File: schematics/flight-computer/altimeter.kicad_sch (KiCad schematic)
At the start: 17 parts, among them U201 NXB0108PW-Q100J, U202 ICM-20789, U203 MS5611-01BA, U204 PCA9306

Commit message: Add order codes for remaining components
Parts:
- C202, C203, C208: Farnell (none) -> 9402047
- R201: Farnell (none) -> 2059185
- R202, R203, R204, R205: Farnell (none) -> 2447187
- U201: Farnell (none) -> 3585605
- U204: Farnell (none) -> 2845091
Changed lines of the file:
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@@
+      (effects (font (size 1.27 1.27)) hide)
+    )
+    (property "Farnell" "2447187" (id 4) (at 129.54 139.7 0)
+      (effects (font (size 1.27 1.27)) hide)
+    )
+    (property "Mouser" "~" (id 5) (at 129.54 139.7 0)
+      (effects (font (size 1.27 1.27)) hide)
+    )
+    (property "RS" "~" (id 6) (at 129.54 139.7 0)
       (effects (font (size 1.27 1.27)) hide)
     )
@@
       (effects (font (size 1.27 1.27)) hide)
     )
+    (property "Mouser" "~" (id 5) (at 176.53 76.2 0)
+      (effects (font (size 1.27 1.27)) hide)
+    )
+    (property "RS" "~" (id 6) (at 176.53 76.2 0)
+      (effects (font (size 1.27 1.27)) hide)
+    )
     (pin "1")
     (pin "2")
@@
       (effects (font (size 1.27 1.27)) hide)
     )
-    (property "Farnell" "" (id 4) (at 105.41 104.14 0)
+    (property "Farnell" "9402047" (id 4) (at 105.41 104.14 0)
+      (effects (font (size 1.27 1.27)) hide)
+    )
+    (property "Mouser" "~" (id 5) (at 105.41 104.14 0)
+      (effects (font (size 1.27 1.27)) hide)
+    )
+    (property "RS" "~" (id 6) (at 105.41 104.14 0)
       (effects (font (size 1.27 1.27)) hide)
     )
@@
     )
     (property "Datasheet" "http://www.ti.com/lit/ds/symlink/pca9306.pdf" (id 3) (at 120.65 135.89 0)
+      (effects (font (size 1.27 1.27)) hide)
+    )
+    (property "Farnell" "2845091" (id 4) (at 113.03 147.32 0)
+      (effects (font (size 1.27 1.27)) hide)
+    )
+    (property "Mouser" "~" (id 5) (at 113.03 147.32 0)
+      (effects (font (size 1.27 1.27)) hide)
+    )
+    (property "RS" "~" (id 6) (at 113.03 147.32 0)
       (effects (font (size 1.27 1.27)) hide)
     )
@@
       (effects (font (size 1.27 1.27)) hide)
     )
+    (property "Mouser" "~" (id 5) (at 162.56 104.14 0)
+      (effects (font (size 1.27 1.27)) hide)
+    )
+    (property "RS" "~" (id 6) (at 162.56 104.14 0)
+      (effects (font (size 1.27 1.27)) hide)
+    )
     (pin "1")
     (pin "2")
@@
     )
     (property "Farnell" "9402047" (id 4) (at 229.87 104.14 0)
+      (effects (font (size 1.27 1.27)) hide)
+    )
+    (property "Mouser" "~" (id 5) (at 229.87 104.14 0)
+      (effects (font (size 1.27 1.27)) hide)
+    )
+    (property "RS" "~" (id 6) (at 229.87 104.14 0)
       (effects (font (size 1.27 1.27)) hide)
     )
@@
       (effects (font (size 1.27 1.27)) hide)
     )
+    (property "Farnell" "2447187" (id 4) (at 132.08 139.7 0)
+      (effects (font (size 1.27 1.27)) hide)
+    )
+    (property "Mouser" "~" (id 5) (at 132.08 139.7 0)
+      (effects (font (size 1.27 1.27)) hide)
+    )
+    (property "RS" "~" (id 6) (at 132.08 139.7 0)
+      (effects (font (size 1.27 1.27)) hide)
+    )
     (pin "1")
     (pin "2")
@@
       (effects (font (size 1.27 1.27)) hide)
     )
-    (property "Farnell" "" (id 4) (at 101.6 156.21 0)
+    (property "Farnell" "9402047" (id 4) (at 101.6 156.21 0)
+      (effects (font (size 1.27 1.27)) hide)
+    )
+    (property "Mouser" "~" (id 5) (at 101.6 156.21 0)
+      (effects (font (size 1.27 1.27)) hide)
+    )
+    (property "RS" "~" (id 6) (at 101.6 156.21 0)
       (effects (font (size 1.27 1.27)) hide)
     )
@@
       (effects (font (size 1.27 1.27)) hide)
     )
+    (property "Mouser" "~" (id 5) (at 157.48 104.14 0)
+      (effects (font (size 1.27 1.27)) hide)
+    )
+    (property "RS" "~" (id 6) (at 157.48 104.14 0)
+      (effects (font (size 1.27 1.27)) hide)
+    )
     (pin "1")
     (pin "2")
@@
     )
     (property "Datasheet" "" (id 3) (at 111.76 60.325 0)
+      (effects (font (size 1.27 1.27)) hide)
+    )
+    (property "Farnell" "3585605" (id 4) (at 111.76 62.23 0)
+      (effects (font (size 1.27 1.27)) hide)
+    )
+    (property "Mouser" "~" (id 5) (at 111.76 62.23 0)
+      (effects (font (size 1.27 1.27)) hide)
+    )
+    (property "RS" "~" (id 6) (at 111.76 62.23 0)
       (effects (font (size 1.27 1.27)) hide)
     )
@@
     )
     (property "Datasheet" "https://3cfeqx1hf82y3xcoull08ihx-wpengine.netdna-ssl.com/wp-content/uploads/2017/10/DS-000169-ICM-20789-TYP-v1.4.pdf" (id 3) (at 162.56 90.17 0)
+      (effects (font (size 1.27 1.27)) hide)
+    )
+    (property "Farnell" "~" (id 4) (at 162.56 62.23 0)
+      (effects (font (size 1.27 1.27)) hide)
+    )
+    (property "Mouser" "~" (id 5) (at 162.56 62.23 0)
+      (effects (font (size 1.27 1.27)) hide)
+    )
+    (property "RS" "~" (id 6) (at 162.56 62.23 0)
       (effects (font (size 1.27 1.27)) hide)
     )
@@
       (effects (font (size 1.27 1.27)) hide)
     )
+    (property "Mouser" "~" (id 5) (at 171.45 104.14 0)
+      (effects (font (size 1.27 1.27)) hide)
+    )
+    (property "RS" "~" (id 6) (at 171.45 104.14 0)
+      (effects (font (size 1.27 1.27)) hide)
+    )
     (pin "1")
     (pin "2")
@@
       (effects (font (size 1.27 1.27)) hide)
     )
-    (property "Farnell" "" (id 4) (at 116.84 104.14 0)
+    (property "Farnell" "9402047" (id 4) (at 116.84 104.14 0)
+      (effects (font (size 1.27 1.27)) hide)
+    )
+    (property "Mouser" "~" (id 5) (at 116.84 104.14 0)
+      (effects (font (size 1.27 1.27)) hide)
+    )
+    (property "RS" "~" (id 6) (at 116.84 104.14 0)
       (effects (font (size 1.27 1.27)) hide)
     )
@@
     )
     (property "Datasheet" "" (id 3) (at 92.71 139.7 0)
+      (effects (font (size 1.27 1.27)) hide)
+    )
+    (property "Farnell" "2447187" (id 4) (at 92.71 139.7 0)
+      (effects (font (size 1.27 1.27)) hide)
+    )
+    (property "Mouser" "~" (id 5) (at 92.71 139.7 0)
+      (effects (font (size 1.27 1.27)) hide)
+    )
+    (property "RS" "~" (id 6) (at 92.71 139.7 0)
       (effects (font (size 1.27 1.27)) hide)
     )
@@
       (effects (font (size 1.27 1.27)) hide)
     )
+    (property "Farnell" "2059185" (id 4) (at 110.49 130.81 0)
+      (effects (font (size 1.27 1.27)) hide)
+    )
+    (property "Mouser" "~" (id 5) (at 110.49 130.81 0)
+      (effects (font (size 1.27 1.27)) hide)
+    )
+    (property "RS" "~" (id 6) (at 110.49 130.81 0)
+      (effects (font (size 1.27 1.27)) hide)
+    )
     (pin "1")
     (pin "2")
@@
       (effects (font (size 1.27 1.27)) hide)
     )
+    (property "Farnell" "2447187" (id 4) (at 90.17 139.7 0)
+      (effects (font (size 1.27 1.27)) hide)
+    )
+    (property "Mouser" "~" (id 5) (at 90.17 139.7 0)
+      (effects (font (size 1.27 1.27)) hide)
+    )
+    (property "RS" "~" (id 6) (at 90.17 139.7 0)
+      (effects (font (size 1.27 1.27)) hide)
+    )
     (pin "1")
     (pin "2")
@@
       (effects (font (size 1.27 1.27)) hide)
     )
+    (property "Farnell" "~" (id 4) (at 227.33 71.12 0)
+      (effects (font (size 1.27 1.27)) hide)
+    )
+    (property "Mouser" "~" (id 5) (at 227.33 71.12 0)
+      (effects (font (size 1.27 1.27)) hide)
+    )
+    (property "RS" "~" (id 6) (at 227.33 71.12 0)
+      (effects (font (size 1.27 1.27)) hide)
+    )

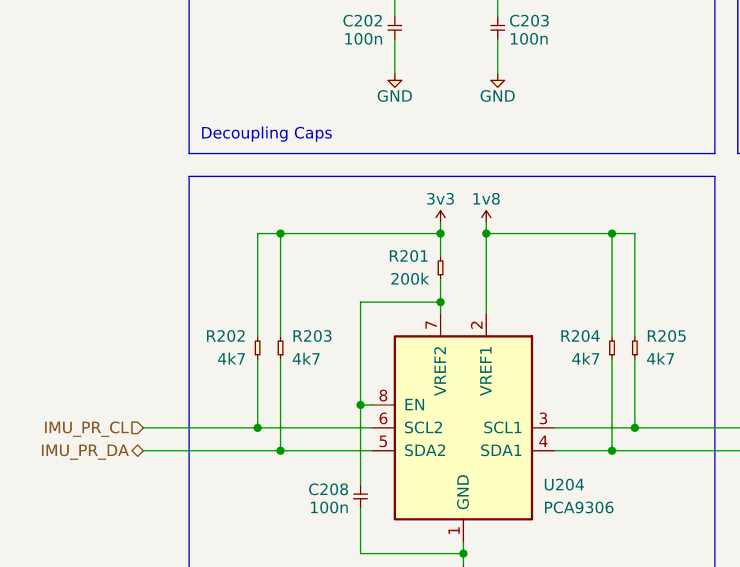
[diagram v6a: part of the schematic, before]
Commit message: Minor changes to pass ERC
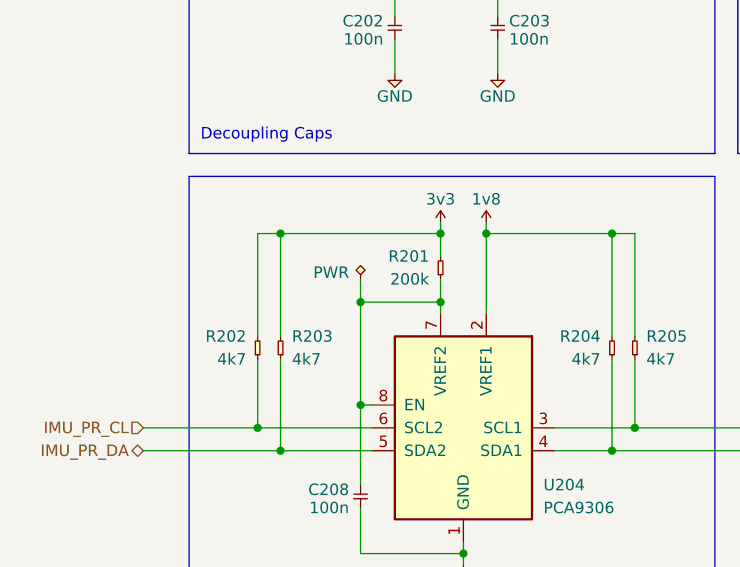
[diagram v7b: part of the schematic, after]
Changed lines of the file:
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@@
   (junction (at 160.02 99.06) (diameter 0) (color 0 0 0 0)
+  )
+  (junction (at 101.6 133.35) (diameter 0) (color 0 0 0 0)
   )
   (junction (at 227.33 81.28) (diameter 0) (color 0 0 0 0)
@@
   )
   (wire (pts (xy 148.59 82.55) (xy 162.56 82.55))
+    (stroke (width 0) (type default) (color 0 0 0 0))
+  )
+  (wire (pts (xy 101.6 130.81) (xy 101.6 133.35))
     (stroke (width 0) (type default) (color 0 0 0 0))
   )
@@
       (effects (font (size 1.27 1.27)) hide)
     )
+    (pin "1")
+  )
+  (symbol (lib_id "Strix:PWR") (at 101.6 130.81 0) (unit 1)
+    (in_bom yes) (on_board yes)
+    (property "Reference" "#FLG0105" (id 0) (at 101.6 126.746 0)
+      (effects (font (size 1.27 1.27)) hide)
+    )
+    (property "Value" "PWR" (id 1) (at 100.33 130.81 0)
+      (effects (font (size 1.27 1.27)) (justify right bottom))
+    )
+    (property "Footprint" "" (id 2) (at 101.6 130.81 0)
+      (effects (font (size 1.27 1.27)) hide)
+    )
+    (property "Datasheet" "" (id 3) (at 101.6 130.81 0)
+      (effects (font (size 1.27 1.27)) hide)
+    )
